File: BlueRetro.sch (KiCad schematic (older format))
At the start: 22 parts, among them J2 Conn_01x19, J3 Conn_01x19, P1 DC Ctrl slot, P1 GC Ctrl slot, P1 N64 Ctrl slot, P2 DC Ctrl slot, P2 GC Ctrl slot, P2 N64 Ctrl slot, P3 DC Ctrl slot, P3 GC Ctrl slot, P3 N64 Ctrl slot, P4 DC Ctrl slot, P4 GC Ctrl slot, P4 N64 Ctrl slot

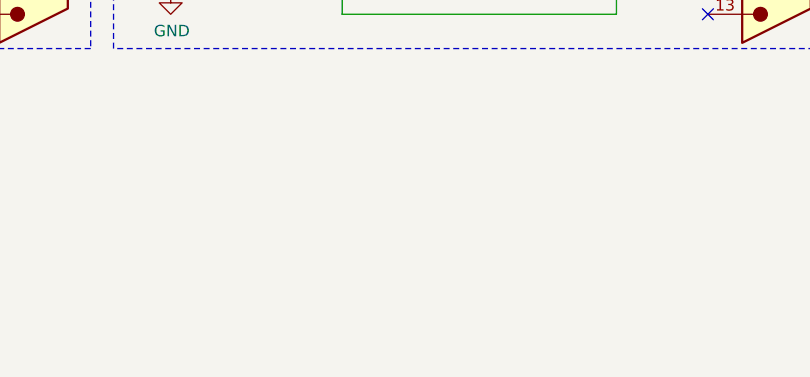
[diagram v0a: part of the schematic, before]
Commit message: Add NES schematic fixup Saturn detect pins
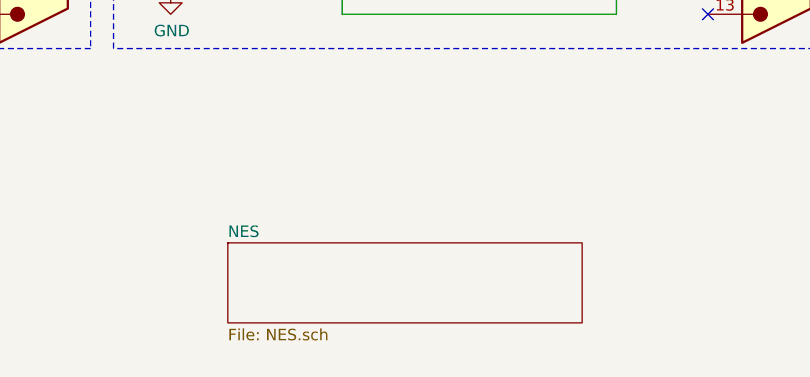
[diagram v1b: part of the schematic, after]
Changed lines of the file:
@@
 $Descr USLetter 11000 8500
 encoding utf-8
-Sheet 1 2
+Sheet 1 3
 Title "BlueRetro"
 Date "2020-05-20"
@@
 F1 "saturn.sch" 50
 $EndSheet
+$Sheet
+S 4350 7450 1550 350
+U 5F1E85DD
+F0 "NES" 50
+F1 "NES.sch" 50
+$EndSheet
 $EndSCHEMATC

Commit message: Correction following first user feedback.
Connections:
- net GND: now also J?.1, J?.1, J?.10, J?.10, J?.10, J?.11, J?.11, J?.11, J?.12, J?.12, J?.12, J?.13, J?.13, J?.13, J?.2, J?.3, J?.3, J?.4, J?.4, J?.4
- net CLK renamed IO14
- net CMD renamed IO15
- net D0 renamed IO2
- net D1 renamed IO4
- net D2 renamed IO12
- net D3 renamed IO13
- no-connect marks 98 -> 78
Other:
- note added: "* Always use external power for this board.\n If using N64 make sure to unplug 3.3v from DB25.\n** Remove R11, R23, R134, R136, R136, R137, R138, R139, R164 & R168\n** Short R12 & R24\n*** Don't short TXD and RXD0"
- note added: "* Require to burn the flash voltage eFuses for avoiding conflict between D2 & MTDI strapping\n**It is important to keep the sd card jumper wire very short (<= 2 inch)\n and plug them directly to the ESP32 pin (not via breadboard).\n**It's critical for the 2 GND on the PMOD to be plug directly to the ESP32 GND pin via short wire!!"
- note added: "ESP-WROVER-KIT V4.1 (PHASE OUT, NOT RECOMMENDED)"
- note added: "ESP32-DevKitC V4 w/ WROOM"
- note removed: "* Always use external power for this board.\n** Remove R11, R23, R134, R136, R136, R137, R138, R139, R164 & R168\n** Short R12 & R24\n*** Don't short TXD and RXD0"
- note removed: "* Require to burn the flash voltage eFuses for avoiding conflict between D2 & MTDI strapping"
- note removed: "ESP-WROVER-KIT V4.1"
- note removed: "ESP32-DevKitC V4"
- moved on the sheet: JP2
